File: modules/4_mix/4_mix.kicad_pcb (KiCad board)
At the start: 2 copper layers, 61 x 68.6 mm, 4 parts

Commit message: Updated the core design
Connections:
- net Net-(5V1-Pin_1) renamed +5V
- GND2 pad 1: GND -> Net-(GND2-Pin_1)
- GND2 pad 2: GND -> Net-(GND2-Pin_1)
- GND2 pad 3: GND -> Net-(GND2-Pin_1)
- GND2 pad 4: GND -> Net-(GND2-Pin_1)
- GND2 pad 5: GND -> Net-(GND2-Pin_1)
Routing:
- net Net-(GND2-Pin_1): track 0.00 -> 10.2 mm
- net GND: track 20.3 -> 10.2 mm
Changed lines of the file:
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@@
 	(net 0 "")
 	(net 1 "GND")
-	(net 2 "Net-(5V1-Pin_1)")
-	(net 3 "Net-(5V2-Pin_1)")
+	(net 2 "Net-(5V2-Pin_1)")
+	(net 3 "+5V")
+	(net 4 "Net-(GND2-Pin_1)")
 	(footprint "Connector_PinHeader_2.54mm:PinHeader_1x05_P2.54mm_Vertical"
 		(layer "B.Cu")
@@
 			(layers "*.Cu" "*.Mask")
 			(remove_unused_layers no)
-			(net 1 "GND")
+			(net 4 "Net-(GND2-Pin_1)")
 			(pinfunction "Pin_1")
 			(pintype "passive")
@@
 			(layers "*.Cu" "*.Mask")
 			(remove_unused_layers no)
-			(net 1 "GND")
+			(net 4 "Net-(GND2-Pin_1)")
 			(pinfunction "Pin_2")
 			(pintype "passive")
@@
 			(layers "*.Cu" "*.Mask")
 			(remove_unused_layers no)
-			(net 1 "GND")
+			(net 4 "Net-(GND2-Pin_1)")
 			(pinfunction "Pin_3")
 			(pintype "passive")
@@
 			(layers "*.Cu" "*.Mask")
 			(remove_unused_layers no)
-			(net 1 "GND")
+			(net 4 "Net-(GND2-Pin_1)")
 			(pinfunction "Pin_4")
 			(pintype "passive")
@@
 			(layers "*.Cu" "*.Mask")
 			(remove_unused_layers no)
-			(net 1 "GND")
+			(net 4 "Net-(GND2-Pin_1)")
 			(pinfunction "Pin_5")
 			(pintype "passive")
@@
 			(layers "*.Cu" "*.Mask")
 			(remove_unused_layers no)
-			(net 2 "Net-(5V1-Pin_1)")
+			(net 3 "+5V")
 			(pinfunction "Pin_1")
 			(pintype "passive")
@@
 			(layers "*.Cu" "*.Mask")
 			(remove_unused_layers no)
-			(net 2 "Net-(5V1-Pin_1)")
+			(net 3 "+5V")
 			(pinfunction "Pin_2")
 			(pintype "passive")
@@
 			(layers "*.Cu" "*.Mask")
 			(remove_unused_layers no)
-			(net 2 "Net-(5V1-Pin_1)")
+			(net 3 "+5V")
 			(pinfunction "Pin_3")
 			(pintype "passive")
@@
 			(layers "*.Cu" "*.Mask")
 			(remove_unused_layers no)
-			(net 2 "Net-(5V1-Pin_1)")
+			(net 3 "+5V")
 			(pinfunction "Pin_4")
 			(pintype "passive")
@@
 			(layers "*.Cu" "*.Mask")
 			(remove_unused_layers no)
-			(net 2 "Net-(5V1-Pin_1)")
+			(net 3 "+5V")
 			(pinfunction "Pin_5")
 			(pintype "passive")
@@
 			(layers "*.Cu" "*.Mask")
 			(remove_unused_layers no)
-			(net 3 "Net-(5V2-Pin_1)")
+			(net 2 "Net-(5V2-Pin_1)")
 			(pinfunction "Pin_1")
 			(pintype "passive")
@@
 			(layers "*.Cu" "*.Mask")
 			(remove_unused_layers no)
-			(net 3 "Net-(5V2-Pin_1)")
+			(net 2 "Net-(5V2-Pin_1)")
 			(pinfunction "Pin_2")
 			(pintype "passive")
@@
 			(layers "*.Cu" "*.Mask")
 			(remove_unused_layers no)
-			(net 3 "Net-(5V2-Pin_1)")
+			(net 2 "Net-(5V2-Pin_1)")
 			(pinfunction "Pin_3")
 			(pintype "passive")
@@
 			(layers "*.Cu" "*.Mask")
 			(remove_unused_layers no)
-			(net 3 "Net-(5V2-Pin_1)")
+			(net 2 "Net-(5V2-Pin_1)")
 			(pinfunction "Pin_4")
 			(pintype "passive")
@@
 			(layers "*.Cu" "*.Mask")
 			(remove_unused_layers no)
-			(net 3 "Net-(5V2-Pin_1)")
+			(net 2 "Net-(5V2-Pin_1)")
 			(pinfunction "Pin_5")
 			(pintype "passive")
@@
 	)
 	(segment
-		(start 86.36 96.52)
-		(end 96.52 96.52)
-		(width 0.2)
-		(layer "F.Cu")
-		(net 1)
-	)
-	(segment
 		(start 55.88 96.52)
 		(end 58.42 96.52)
@@
 	)
 	(segment
+		(start 86.36 53.34)
+		(end 96.52 53.34)
+		(width 0.2)
+		(layer "F.Cu")
+		(net 2)
+	)
+	(segment
 		(start 55.88 53.34)
 		(end 66.04 53.34)
 		(width 0.2)
 		(layer "F.Cu")
-		(net 2)
+		(net 3)
 	)
 	(segment
-		(start 86.36 53.34)
-		(end 96.52 53.34)
+		(start 86.36 96.52)
+		(end 96.52 96.52)
 		(width 0.2)
 		(layer "F.Cu")
-		(net 3)
+		(net 4)
 	)
 )

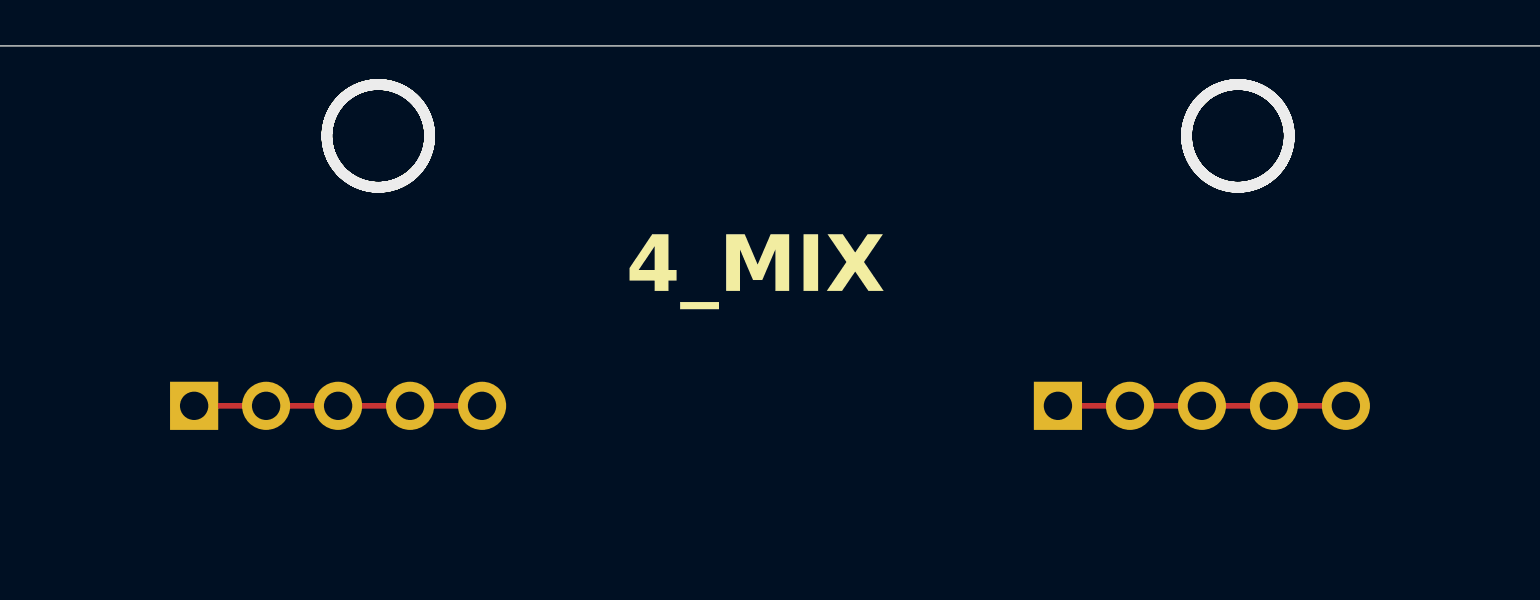
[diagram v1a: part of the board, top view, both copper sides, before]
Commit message: Fixed some pcb layout issues.
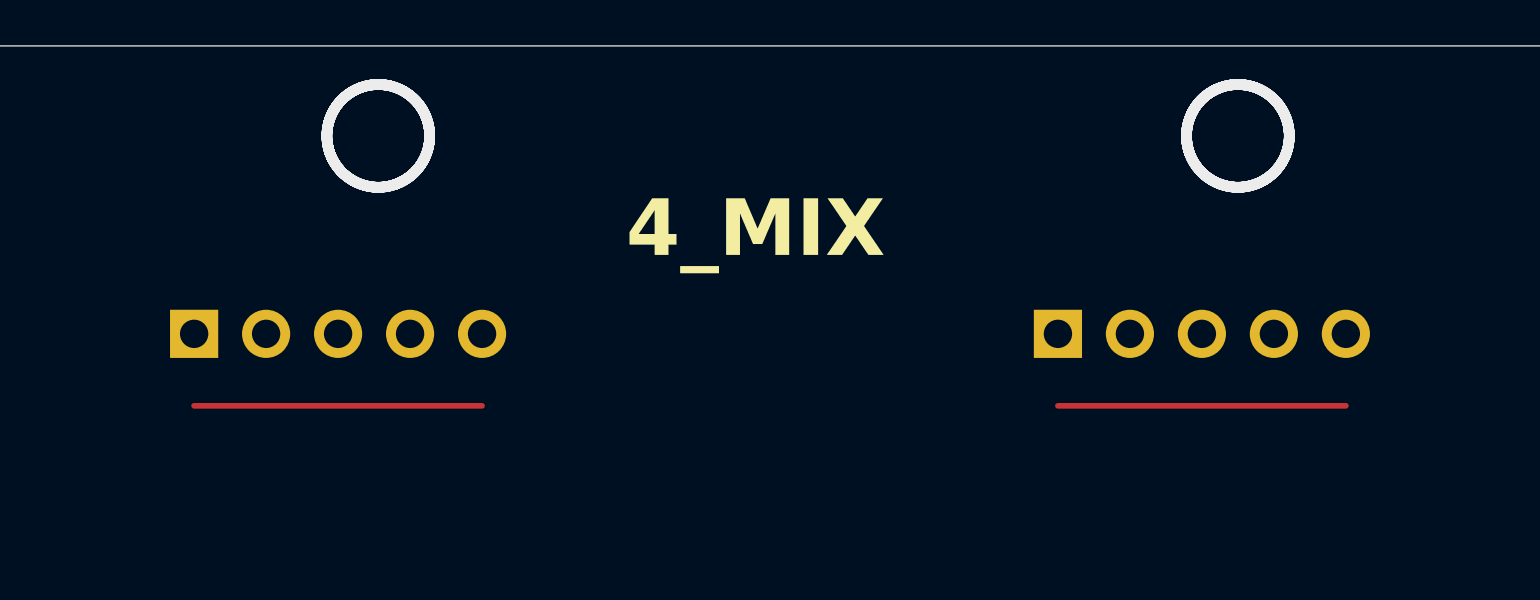
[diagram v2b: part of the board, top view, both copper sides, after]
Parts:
- moved 5V1 2.54 mm to (55.9, 50.8)
- moved 5V2 2.54 mm to (86.4, 50.8)
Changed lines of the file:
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@@
 	(footprint "Connector_PinHeader_2.54mm:PinHeader_1x05_P2.54mm_Vertical"
 		(layer "B.Cu")
-		(at 55.88 53.34 -90)
+		(at 55.88 50.8 -90)
 		(descr "Through hole straight pin header, 1x05, 2.54mm pitch, single row")
 		(tags "Through hole pin header THT 1x05 2.54mm single row")
@@
 	(footprint "Connector_PinHeader_2.54mm:PinHeader_1x05_P2.54mm_Vertical"
 		(layer "B.Cu")
-		(at 86.36 53.34 -90)
+		(at 86.36 50.8 -90)
 		(descr "Through hole straight pin header, 1x05, 2.54mm pitch, single row")
 		(tags "Through hole pin header THT 1x05 2.54mm single row")
@@
 		)
 		(fp_text user "${REFERENCE}"
-			(at 0 -5.08 360)
+			(at 0 -5.08 0)
 			(layer "B.Fab")
 			(effects
@@
 	)
 	(gr_text "4_MIX"
-		(at 71.12 49.53 0)
+		(at 71.12 48.26 0)
 		(layer "F.SilkS")
 		(effects

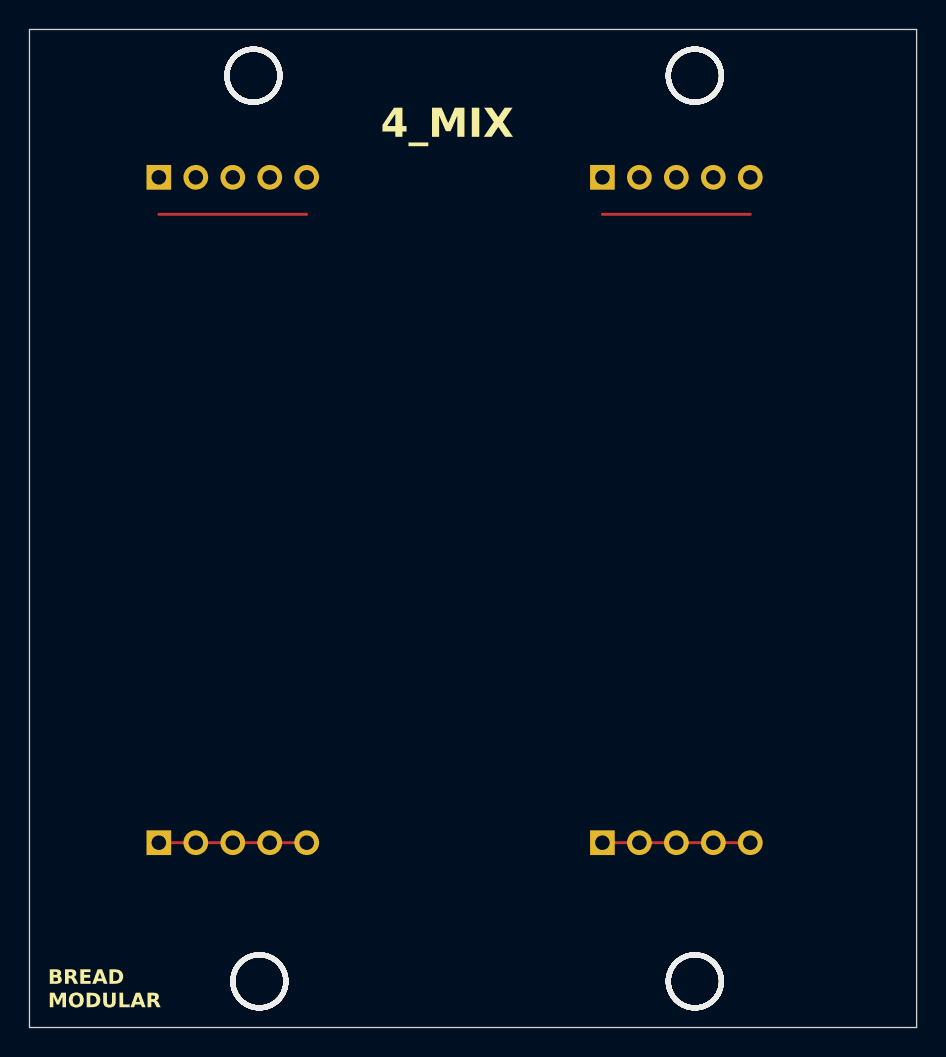
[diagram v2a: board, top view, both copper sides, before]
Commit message: Add the full mixer
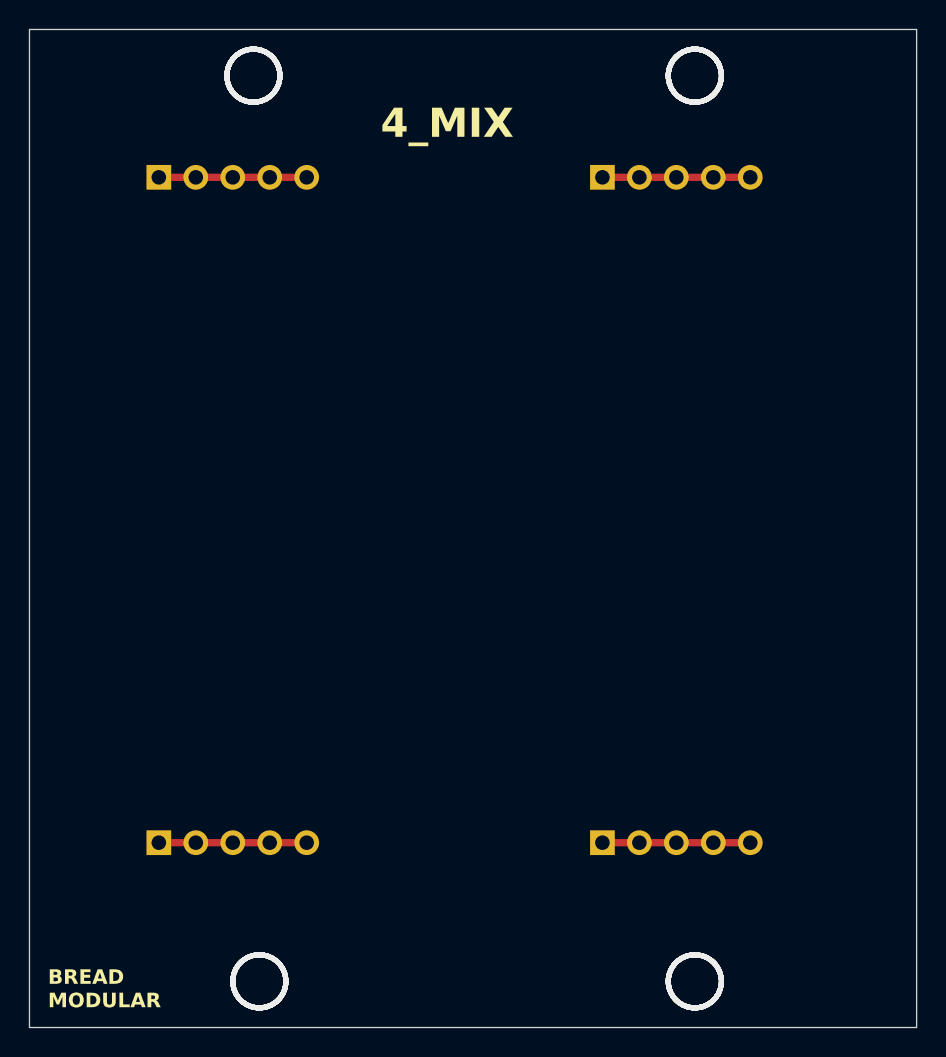
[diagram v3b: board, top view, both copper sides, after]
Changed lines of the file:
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@@
 	)
 	(segment
-		(start 58.42 96.52)
+		(start 55.88 96.52)
 		(end 66.04 96.52)
-		(width 0.2)
+		(width 0.5)
 		(layer "F.Cu")
 		(net 1)
 	)
 	(segment
-		(start 55.88 96.52)
-		(end 58.42 96.52)
-		(width 0.2)
-		(layer "F.Cu")
-		(net 1)
-	)
-	(segment
-		(start 86.36 53.34)
-		(end 96.52 53.34)
-		(width 0.2)
+		(start 86.36 50.8)
+		(end 96.52 50.8)
+		(width 0.5)
 		(layer "F.Cu")
 		(net 2)
 	)
 	(segment
-		(start 55.88 53.34)
-		(end 66.04 53.34)
-		(width 0.2)
+		(start 55.88 50.8)
+		(end 66.04 50.8)
+		(width 0.5)
 		(layer "F.Cu")
 		(net 3)
@@
 		(start 86.36 96.52)
 		(end 96.52 96.52)
-		(width 0.2)
+		(width 0.5)
 		(layer "F.Cu")
 		(net 4)

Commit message: Implemented the PCB design of 4_mix
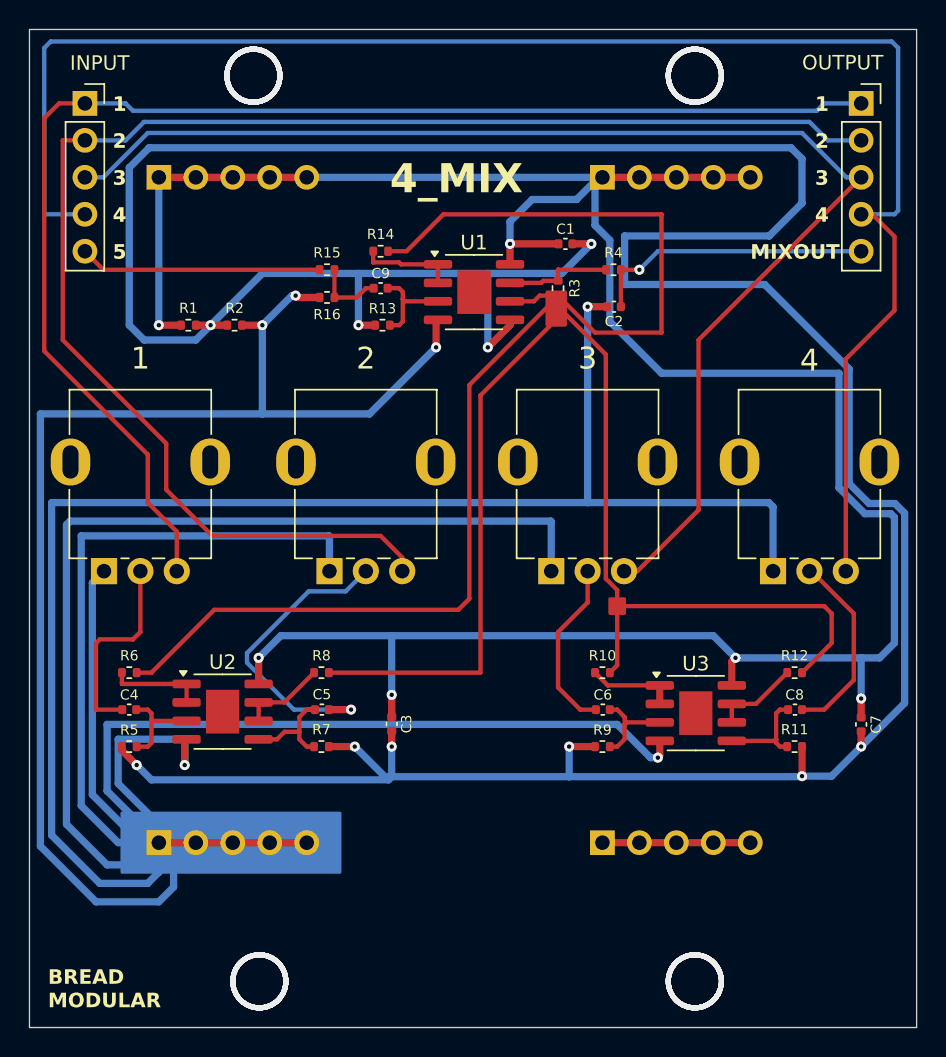
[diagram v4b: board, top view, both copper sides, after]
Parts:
- added 1: 50k, BreadModular_OPT1:Potentiometer_RV09, F.Cu at (52.1, 77.9)
- added 2: 50k, BreadModular_OPT1:Potentiometer_RV09, F.Cu at (67.6, 77.9)
- added 3: 50k, BreadModular_OPT1:Potentiometer_RV09, F.Cu at (82.8, 77.9)
- added 4: 50k, BreadModular_OPT1:Potentiometer_RV09, F.Cu at (98.1, 77.9)
- added C1: 0.1uf, Capacitor_SMD:C_0402_1005Metric, F.Cu at (83.8, 55.4)
- added C2: 0.01uf, Capacitor_SMD:C_0402_1005Metric, F.Cu at (87.2, 59.7)
- added C3: 0.1uf, Capacitor_SMD:C_0402_1005Metric, F.Cu at (71.9, 88.4)
- added C4: 0.1uf, Capacitor_SMD:C_0402_1005Metric, F.Cu at (53.8, 87.4)
- added C5: 0.1uf, Capacitor_SMD:C_0402_1005Metric, F.Cu at (67.1, 87.4)
- added C6: 0.1uf, Capacitor_SMD:C_0402_1005Metric, F.Cu at (86.4, 87.4)
- added C7: 0.1uf, Capacitor_SMD:C_0402_1005Metric, F.Cu at (104.1, 88.4)
- added C8: 0.1uf, Capacitor_SMD:C_0402_1005Metric, F.Cu at (99.6, 87.4)
- added C9: 0.1uf, Capacitor_SMD:C_0402_1005Metric, F.Cu at (71.1, 58.4)
- added INPUT: Conn_01x05_Socket, Connector_PinSocket_2.54mm:PinSocket_1x05_P2.54mm_Vertical, F.Cu at (50.8, 45.7)
- added OUTPUT: Conn_01x05_Socket, Connector_PinSocket_2.54mm:PinSocket_1x05_P2.54mm_Vertical, F.Cu at (104.1, 45.7)
- added R1: 1k, Resistor_SMD:R_0402_1005Metric, F.Cu at (57.9, 61.0)
- added R10: 100k, Resistor_SMD:R_0402_1005Metric, F.Cu at (86.4, 84.8)
- added R11: 100k, Resistor_SMD:R_0402_1005Metric, F.Cu at (99.6, 89.9)
- added R12: 100k, Resistor_SMD:R_0402_1005Metric, F.Cu at (99.6, 84.8)
- added R13: 100k, Resistor_SMD:R_0402_1005Metric, F.Cu at (71.2, 61.0)
- added R14: 100k, Resistor_SMD:R_0402_1005Metric, F.Cu at (71.1, 55.9)
- added R15: 1k, Resistor_SMD:R_0402_1005Metric, F.Cu at (67.4, 57.1)
- added R16: 51k, Resistor_SMD:R_0402_1005Metric, F.Cu at (67.4, 59.1)
- added R2: 1k, Resistor_SMD:R_0402_1005Metric, F.Cu at (61.1, 61.0)
- added R3: 100k, Resistor_SMD:R_0402_1005Metric, F.Cu at (83.3, 58.4)
- added R4: 1k, Resistor_SMD:R_0402_1005Metric, F.Cu at (87.1, 57.1)
- added R5: 100k, Resistor_SMD:R_0402_1005Metric, F.Cu at (53.8, 89.9)
- added R6: 100k, Resistor_SMD:R_0402_1005Metric, F.Cu at (53.8, 84.8)
- added R7: 100k, Resistor_SMD:R_0402_1005Metric, F.Cu at (67.1, 89.9)
- added R8: 100k, Resistor_SMD:R_0402_1005Metric, F.Cu at (67.1, 84.8)
- added R9: 100k, Resistor_SMD:R_0402_1005Metric, F.Cu at (86.4, 89.9)
- added U1: LM358, Package_SO:SOIC-8-1EP_3.9x4.9mm_P1.27mm_EP2.29x3mm, F.Cu at (77.5, 58.7)
- added U2: LM358, Package_SO:SOIC-8-1EP_3.9x4.9mm_P1.27mm_EP2.29x3mm, F.Cu at (60.3, 87.5)
- added U3: LM358, Package_SO:SOIC-8-1EP_3.9x4.9mm_P1.27mm_EP2.29x3mm, F.Cu at (92.8, 87.6)
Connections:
- 5V2 pad 1: Net-(5V2-Pin_1) -> +5V
- 5V2 pad 2: Net-(5V2-Pin_1) -> +5V
- 5V2 pad 3: Net-(5V2-Pin_1) -> +5V
- 5V2 pad 4: Net-(5V2-Pin_1) -> +5V
- 5V2 pad 5: Net-(5V2-Pin_1) -> +5V
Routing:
- net GND: track 10.2 -> 398.6 mm, vias 0 -> 6
- net 2.5V: track 0.00 -> 243.8 mm, vias 0 -> 10
- net Net-(U1B--): track 0.00 -> 173.1 mm
- net +5V: track 10.2 -> 174.0 mm, vias 0 -> 6
- net IN_4: track 0.00 -> 114.4 mm
- net IN_2: track 0.00 -> 101.9 mm
- net IN_1: track 0.00 -> 91.9 mm
- net IN_3: track 0.00 -> 90.2 mm
- net Net-(C5-Pad1): track 0.00 -> 21.2 mm, vias 0 -> 1
- net MIXOUT: track 0.00 -> 19.6 mm, vias 0 -> 1
- net IN_5: track 0.00 -> 16.7 mm
- net Net-(C4-Pad1): track 0.00 -> 13.9 mm
- net Net-(C8-Pad1): track 0.00 -> 13.2 mm
- net Net-(C6-Pad1): track 0.00 -> 12.1 mm
- net Net-(5V2-Pin_1): track 10.2 -> 0.00 mm
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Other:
- board text added: "1"
- board text added: "2"
- board text added: "3"
- board text added: "4"
- board text added: "5"
- board text added: "MIXOUT"

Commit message: Change some routing rules.
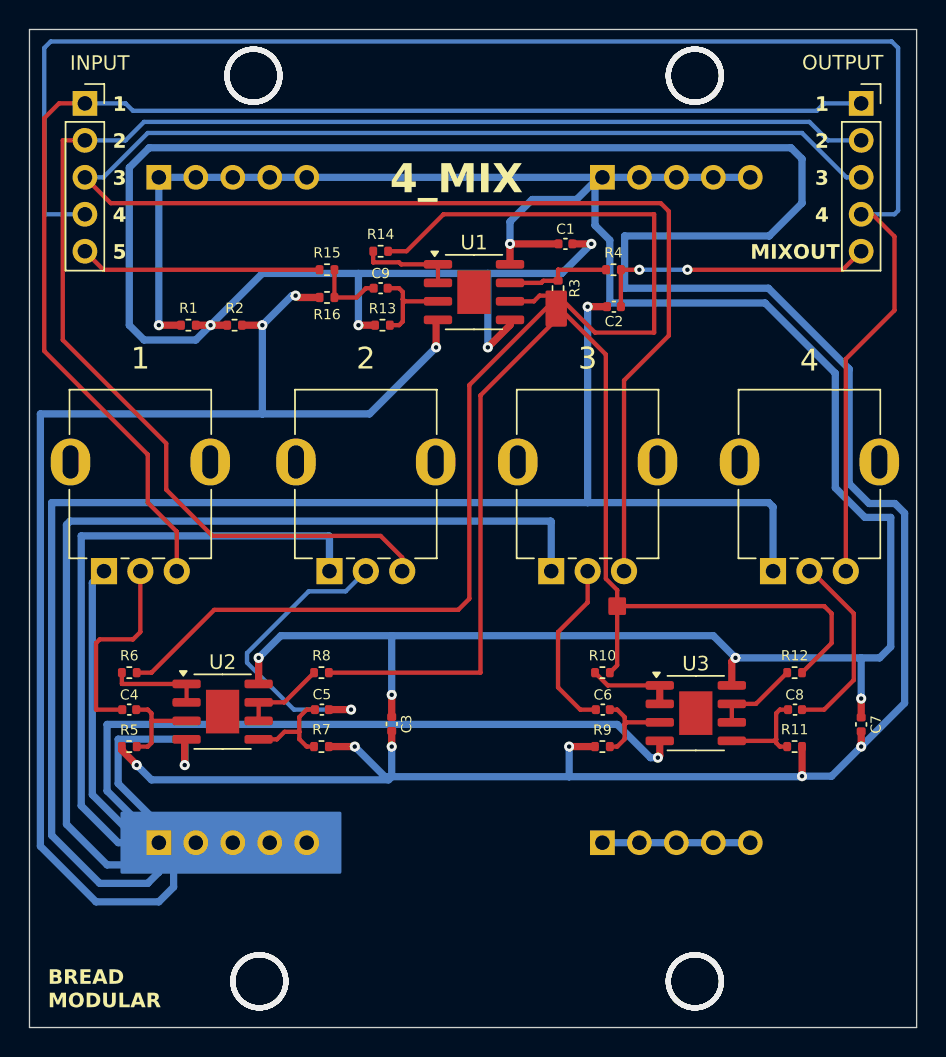
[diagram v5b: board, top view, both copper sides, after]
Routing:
- net IN_3: track 90.2 -> 123.0 mm
- net +5V: track 174.0 -> 172.9 mm
- net Net-(U1B--): track 173.1 -> 172.1 mm
- net MIXOUT: vias 1 -> 2

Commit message: Finalized 4_mix for production
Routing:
- net IN_4: track 114.4 -> 109.9 mm
